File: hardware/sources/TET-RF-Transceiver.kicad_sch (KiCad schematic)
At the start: 26 parts, among them U11 SMA_1, U12 W25Q128JVSIQTR, U13 W25Q128JVSIQTR, U14 E80-900M2213S, U15 SMA_2, U16 W25Q128JVSIQTR, U17 TMP112AIDRLR, U18 INA226AQDGSRQ1, U19 TMP112AIDRLR

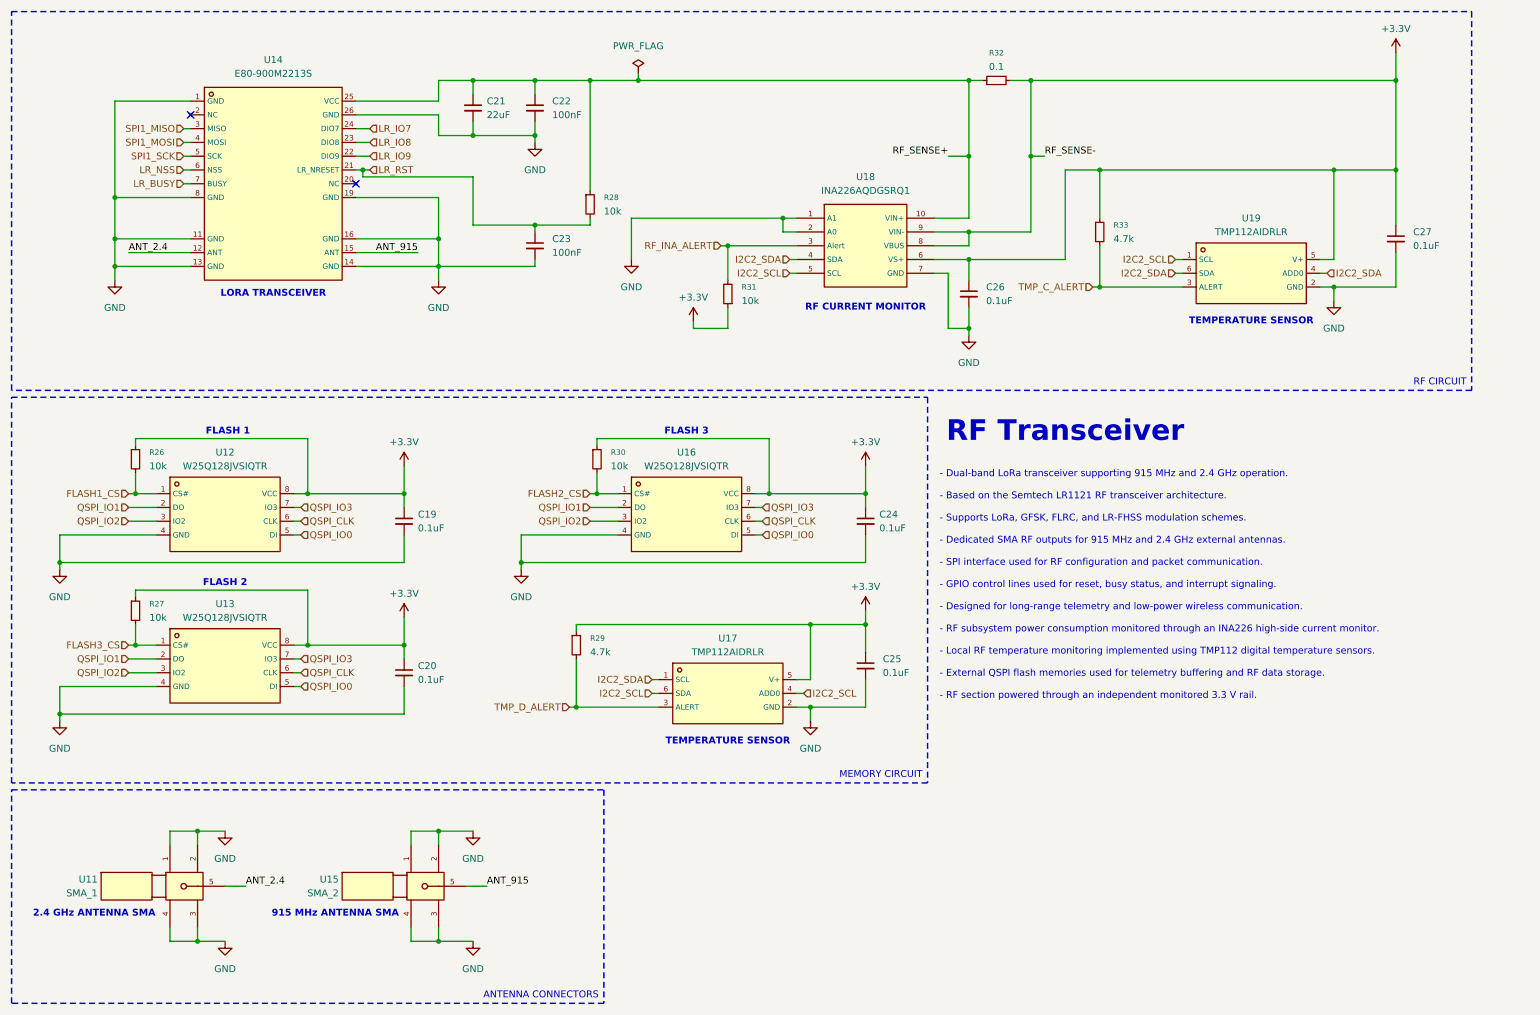
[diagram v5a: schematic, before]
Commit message: feat(schematic): fix double pull-up resistor for LR_BUSY
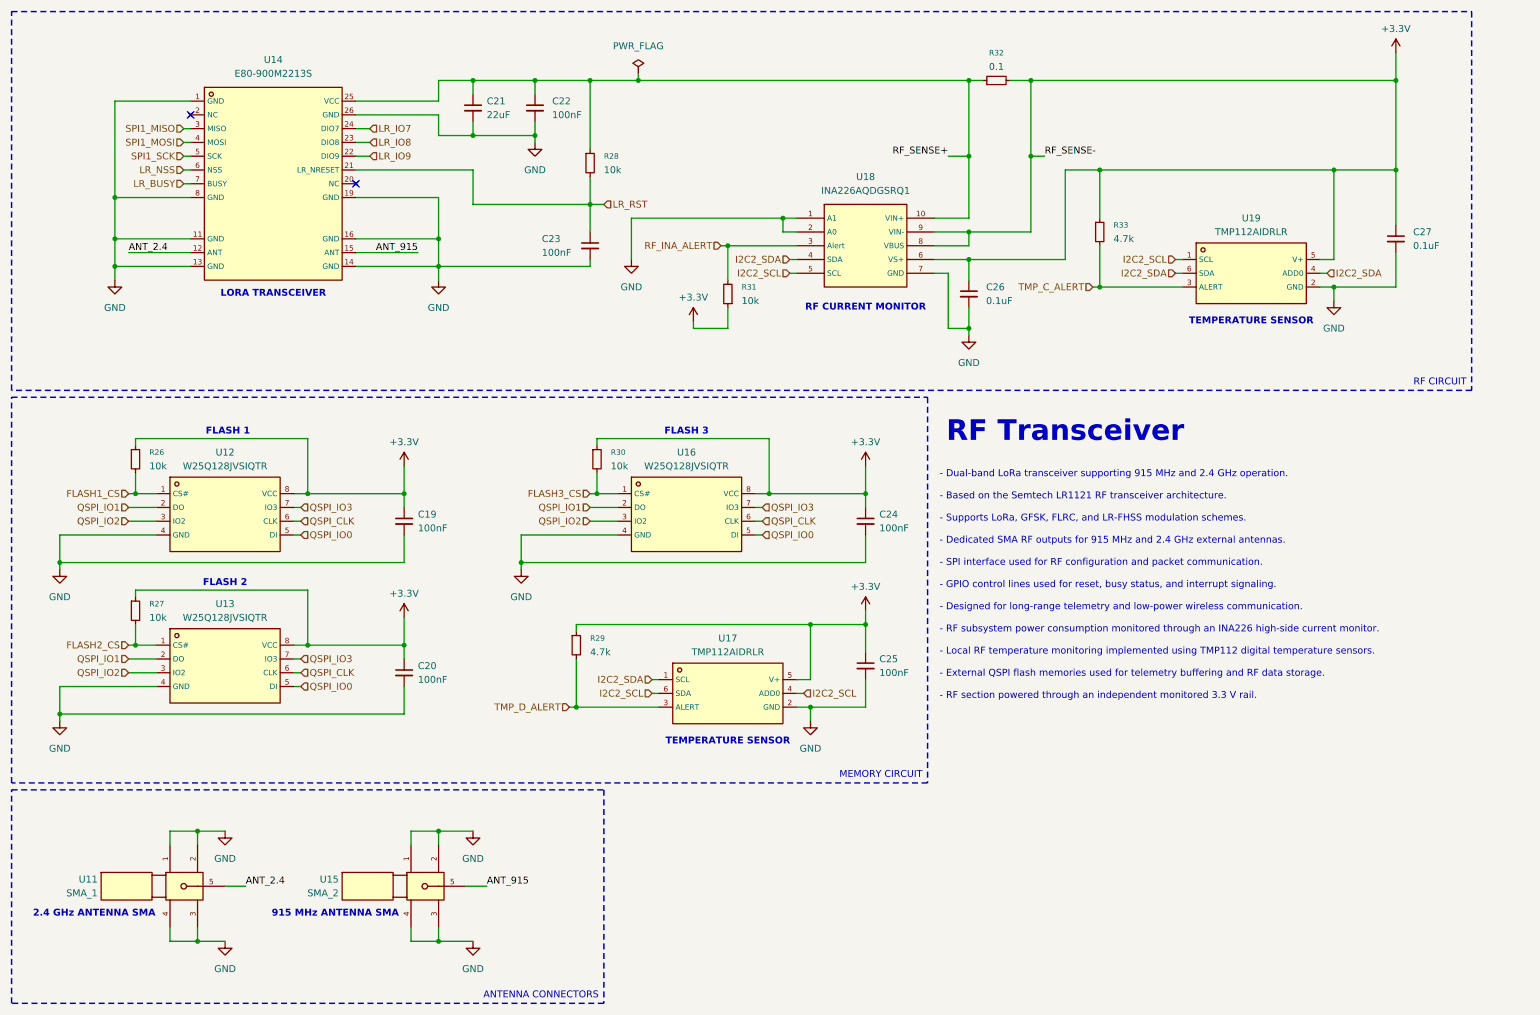
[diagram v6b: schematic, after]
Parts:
- C19, C20, C24, C25: value 0.1uF -> 100nF
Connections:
- net FLASH2_CS: now also R27.2, U13.1 (CS#); no longer R30.2, U16.1 (CS#)
- net FLASH3_CS: now also R30.2, U16.1 (CS#); no longer R27.2, U13.1 (CS#)
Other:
- moved on the sheet: C23, R28
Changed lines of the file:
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@@
 	)
 	(junction
+		(at 120.65 49.53)
+		(diameter 0)
+		(color 0 0 0 0)
+	)
+	(junction
 		(at 153.67 102.87)
 		(diameter 0)
@@
 	)
 	(junction
-		(at 120.65 26.67)
-		(diameter 0)
-		(color 0 0 0 0)
-	)
-	(junction
 		(at 36.83 102.87)
 		(diameter 0)
@@
 	)
 	(junction
+		(at 120.65 26.67)
+		(diameter 0)
+		(color 0 0 0 0)
+	)
+	(junction
 		(at 33.02 48.26)
 		(diameter 0)
@@
 	)
 	(junction
-		(at 110.49 53.34)
-		(diameter 0)
-		(color 0 0 0 0)
-	)
-	(junction
 		(at 161.29 127)
 		(diameter 0)
@@
 	)
 	(junction
-		(at 78.74 43.18)
-		(diameter 0)
-		(color 0 0 0 0)
-	)
-	(junction
 		(at 190.5 59.69)
 		(diameter 0)
@@
 	(wire
 		(pts
-			(xy 99.06 44.45) (xy 99.06 53.34)
+			(xy 99.06 43.18) (xy 99.06 49.53)
 		)
 		(stroke
@@
 	(wire
 		(pts
-			(xy 78.74 43.18) (xy 80.01 43.18)
-		)
-		(stroke
-			(width 0)
-			(type default)
-		)
-	)
-	(wire
-		(pts
 			(xy 269.24 58.42) (xy 269.24 64.77)
 		)
@@
 	(wire
 		(pts
-			(xy 110.49 60.96) (xy 110.49 59.69)
+			(xy 120.65 60.96) (xy 120.65 59.69)
 		)
 		(stroke
@@
 	(wire
 		(pts
-			(xy 120.65 26.67) (xy 120.65 46.99)
+			(xy 120.65 26.67) (xy 120.65 39.37)
 		)
 		(stroke
@@
 	(wire
 		(pts
-			(xy 92.71 60.96) (xy 110.49 60.96)
+			(xy 92.71 60.96) (xy 120.65 60.96)
 		)
 		(stroke
@@
 	(wire
 		(pts
-			(xy 120.65 53.34) (xy 110.49 53.34)
-		)
-		(stroke
-			(width 0)
-			(type default)
-		)
-	)
-	(wire
-		(pts
 			(xy 92.71 165.1) (xy 87.63 165.1)
 		)
@@
 	(wire
 		(pts
-			(xy 78.74 44.45) (xy 99.06 44.45)
-		)
-		(stroke
-			(width 0)
-			(type default)
-		)
-	)
-	(wire
-		(pts
 			(xy 99.06 185.42) (xy 92.71 185.42)
 		)
@@
 	(wire
 		(pts
-			(xy 99.06 53.34) (xy 110.49 53.34)
+			(xy 99.06 49.53) (xy 120.65 49.53)
 		)
 		(stroke
@@
 	(wire
 		(pts
-			(xy 110.49 53.34) (xy 110.49 54.61)
-		)
-		(stroke
-			(width 0)
-			(type default)
-		)
-	)
-	(wire
-		(pts
 			(xy 86.36 97.79) (xy 86.36 102.87)
 		)
@@
 	(wire
 		(pts
+			(xy 120.65 49.53) (xy 120.65 54.61)
+		)
+		(stroke
+			(width 0)
+			(type default)
+		)
+	)
+	(wire
+		(pts
 			(xy 35.56 135.89) (xy 40.64 135.89)
 		)
@@
 	(wire
 		(pts
-			(xy 120.65 52.07) (xy 120.65 53.34)
+			(xy 120.65 44.45) (xy 120.65 49.53)
 		)
 		(stroke
@@
 	(wire
 		(pts
+			(xy 123.19 49.53) (xy 120.65 49.53)
+		)
+		(stroke
+			(width 0)
+			(type default)
+		)
+	)
+	(wire
+		(pts
 			(xy 190.5 72.39) (xy 186.69 72.39)
 		)
@@
 	(wire
 		(pts
-			(xy 78.74 43.18) (xy 78.74 44.45)
-		)
-		(stroke
-			(width 0)
-			(type default)
-		)
-	)
-	(wire
-		(pts
 			(xy 158.75 139.7) (xy 160.02 139.7)
 		)
@@
 	(wire
 		(pts
-			(xy 78.74 43.18) (xy 77.47 43.18)
+			(xy 77.47 43.18) (xy 99.06 43.18)
 		)
 		(stroke
@@
 		)
 	)
+	(hierarchical_label "LR_RST"
+		(shape input)
+		(at 123.19 49.53 0)
+		(effects
+			(font
+				(size 1.27 1.27)
+			)
+			(justify left)
+		)
+	)
 	(hierarchical_label "LR_IO7"
 		(shape input)
@@
 		)
 	)
-	(hierarchical_label "LR_RST"
-		(shape input)
-		(at 80.01 43.18 0)
-		(effects
-			(font
-				(size 1.27 1.27)
-			)
-			(justify left)
-		)
-	)
 	(hierarchical_label "QSPI_CLK"
 		(shape input)
@@
 		)
 	)
-	(hierarchical_label "FLASH3_CS"
+	(hierarchical_label "FLASH2_CS"
 		(shape input)
 		(at 35.56 130.81 180)
@@
 		)
 	)
-	(hierarchical_label "FLASH2_CS"
+	(hierarchical_label "FLASH3_CS"
 		(shape input)
 		(at 120.65 102.87 180)
@@
 	(symbol
 		(lib_id "Device:R_Small")
-		(at 120.65 49.53 0)
+		(at 120.65 41.91 0)
 		(unit 1)
 		(body_style 1)
@@
 		(fields_autoplaced yes)
 		(property "Reference" "R28"
-			(at 123.19 48.2599 0)
+			(at 123.19 40.6399 0)
 			(show_name no)
 			(do_not_autoplace no)
@@
 		)
 		(property "Value" "10k"
-			(at 123.19 50.7999 0)
+			(at 123.19 43.1799 0)
 			(show_name no)
 			(do_not_autoplace no)
@@
 		)
 		(property "Footprint" "Resistor_SMD:R_0603_1608Metric"
-			(at 120.65 49.53 0)
+			(at 120.65 41.91 0)
 			(hide yes)
 			(show_name no)
@@
 		)
 		(property "Datasheet" ""
-			(at 120.65 49.53 0)
+			(at 120.65 41.91 0)
 			(hide yes)
 			(show_name no)
@@
 		)
 		(property "Description" "Resistor, small symbol"
-			(at 120.65 49.53 0)
+			(at 120.65 41.91 0)
 			(hide yes)
 			(show_name no)
@@
 			)
 		)
-		(property "Value" "0.1uF"
+		(property "Value" "100nF"
 			(at 88.9 109.2262 0)
 			(show_name no)
@@
 		(fields_autoplaced yes)
 		(property "Reference" "C25"
-			(at 174.625 133.3562 0)
+			(at 173.99 133.3562 0)
 			(show_name no)
 			(do_not_autoplace no)
@@
 			)
 		)
-		(property "Value" "0.1uF"
-			(at 174.625 135.8962 0)
+		(property "Value" "100nF"
+			(at 173.99 135.8962 0)
 			(show_name no)
 			(do_not_autoplace no)
@@
 			)
 		)
-		(property "Value" "0.1uF"
+		(property "Value" "100nF"
 			(at 88.9 137.1662 0)
 			(show_name no)
@@
 	(symbol
 		(lib_id "Device:C_Small")
-		(at 110.49 57.15 0)
+		(at 120.65 57.15 0)
 		(unit 1)
 		(body_style 1)
@@
 		(in_pos_files yes)
 		(dnp no)
-		(fields_autoplaced yes)
 		(property "Reference" "C23"
-			(at 113.665 55.8862 0)
+			(at 111.76 55.88 0)
 			(show_name no)
 			(do_not_autoplace no)
@@
 		)
 		(property "Value" "100nF"
-			(at 113.665 58.4262 0)
+			(at 111.76 58.42 0)
 			(show_name no)
 			(do_not_autoplace no)
@@
 		)
 		(property "Footprint" "Capacitor_SMD:C_0603_1608Metric"
-			(at 110.49 57.15 0)
+			(at 120.65 57.15 0)
 			(hide yes)
 			(show_name no)
@@
 		)
 		(property "Datasheet" ""
-			(at 110.49 57.15 0)
+			(at 120.65 57.15 0)
 			(hide yes)
 			(show_name no)
@@
 		)
 		(property "Description" "Unpolarized capacitor, small symbol"
-			(at 110.49 57.15 0)
+			(at 120.65 57.15 0)
 			(hide yes)
 			(show_name no)
@@
 			)
 		)
-		(property "Value" "0.1uF"
+		(property "Value" "100nF"
 			(at 173.99 109.2262 0)
 			(show_name no)

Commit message: hardware(pcb_design): components Micro-Placement
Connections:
- net RF_SENSE+ is gone; now on net +3.3V: C21.1, C22.1, R28.1, R32.1, U14.25 (VCC), U18.10 (VIN+)
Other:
- moved on the sheet: R32
